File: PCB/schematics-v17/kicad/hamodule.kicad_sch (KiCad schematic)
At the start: 85 parts, among them J1 2604-1104, J10 EspSense, J11 Conn_01x02_Male, J12 DoNotCon->, J2 2604-1102, J3 USB_C_Receptacle_USB2.0, J4 ESP Relays, J5 Current Jumper, J6 GND 3.3V, J7 Conn_01x02, J8 Current Jumper, J9 2604-1104, K1 PCN-105D, K2 PCN-105D, K3 PCN-105D, K4 PCN-105D, Q1 SS8050-SMD, Q2 SS8050, SW1 EN, SW2 IO0, U1 ULN2003A, U2 ESP32-WROOM-32E, U4 LD1117AV33_TO220, U5 MCP9700T-ETT, U6 LDA210-PDIP, U7 LDA210-PDIP, U8 CP2102N-A01-GQFN28

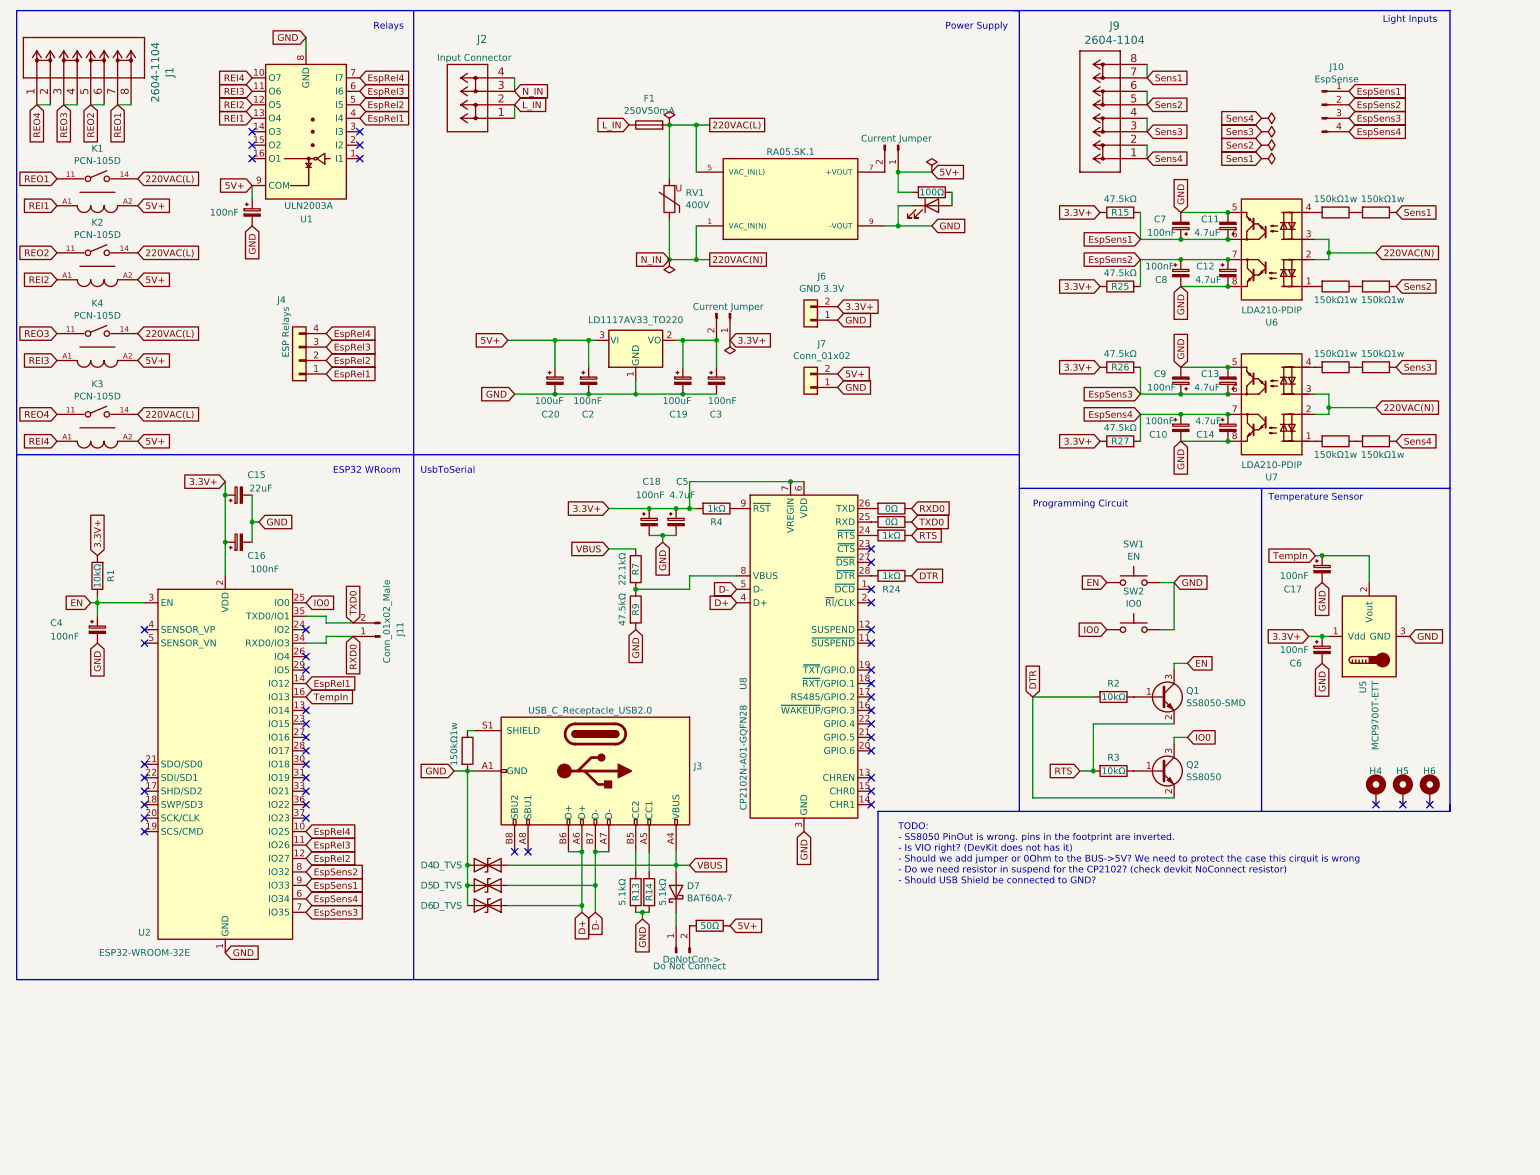
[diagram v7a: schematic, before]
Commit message: temp sensor GPIO is not compatible with Wifi! Crap, I should have tested this
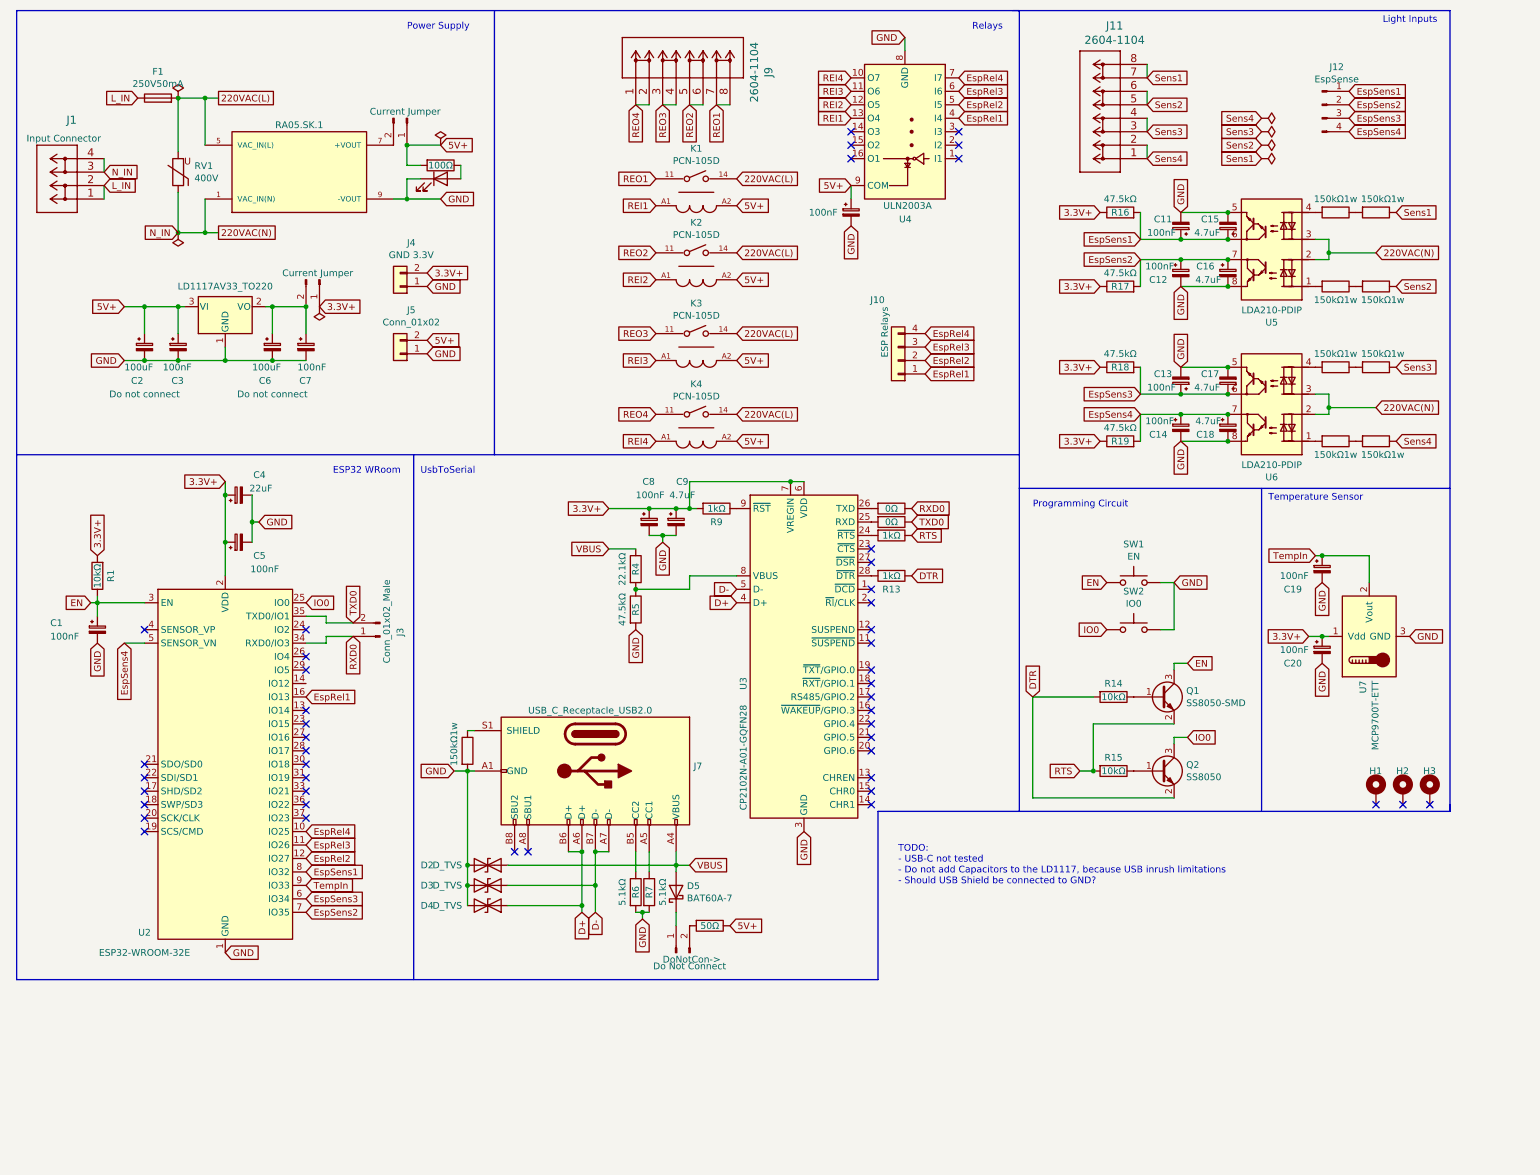
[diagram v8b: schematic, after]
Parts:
- C2: renamed from C20; Field4 (none) -> Do not connect
- C6: renamed from C19; Field4 (none) -> Do not connect
- J12: renamed from J10; footprint Connector_PinSocket_2.00mm:PinSocket_1x04_P2.00mm_Vertical -> Connector_PinSocket_2.54mm:PinSocket_1x04_P2.54mm_Vertical
- J3: renamed from J11; footprint Connector_PinHeader_2.00mm:PinHeader_1x02_P2.00mm_Vertical -> Connector_PinHeader_2.54mm:PinHeader_1x02_P2.54mm_Vertical; Field4 (none) -> Rx | Tx
- renumbered C4 to C1, C1 to C10, C7 to C11, C8 to C12, C9 to C13, C10 to C14, C11 to C15, C12 to C16, C13 to C17, C14 to C18, C17 to C19, C6 to C20, C2 to C3, C15 to C4, C16 to C5, C3 to C7, C18 to C8, C5 to C9, D2 to D1, D4 to D2, D5 to D3, D6 to D4, D7 to D5, H4 to H1, H5 to H2, H6 to H3, J2 to J1, J4 to J10, J9 to J11, J5 to J2, J6 to J4, J7 to J5, J8 to J6, J3 to J7, J12 to J8, J1 to J9, K4 to K3, K3 to K4, R8 to R10, R6 to R11, R5 to R12, R24 to R13, R2 to R14, R3 to R15, R15 to R16, R25 to R17, R26 to R18, R27 to R19, R11 to R2, R16 to R20, R17 to R21, R18 to R22, R19 to R23, R20 to R24, R21 to R25, R22 to R26, R23 to R27, R12 to R3, R7 to R4, R9 to R5, R13 to R6, R14 to R7, R10 to R8, R4 to R9, U4 to U1, U8 to U3, U1 to U4, U6 to U5, U7 to U6, U5 to U7
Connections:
- net EspRel1: now also U2.16 (IO13); no longer U2.14 (IO12)
- net EspSens1: now also U2.8 (IO32); no longer U2.9 (IO33)
- net EspSens2: now also U2.7 (IO35); no longer U2.8 (IO32)
- net EspSens3: now also U2.6 (IO34); no longer U2.7 (IO35)
- net EspSens4: now also U2.5 (SENSOR_VN); no longer U2.6 (IO34)
- net TempIn: now also U2.9 (IO33); no longer U2.16 (IO13)
- no-connect marks 47 -> 46
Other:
- note added: "TODO: - USB-C not tested - Do not add Capacitors to the LD1117, because USB inrush limitations - Should USB Shield be connected to GND?"
- note removed: "TODO: - SS8050 PinOut is wrong. pins in the footprint are inverted. - Is VIO right? (DevKit does not has it) - Should we add jumper or 0Ohm to the BUS->5V? We need to protect the case this cirquit is wrong - Do we need resistor in suspend for the CP2102? (check devkit NoConnect resistor) - Should USB Shield be connected to GND?"
- moved on the sheet: C2, C3, C6, C7, F1, J1, J10, J4, J5, J9, K1, K2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
